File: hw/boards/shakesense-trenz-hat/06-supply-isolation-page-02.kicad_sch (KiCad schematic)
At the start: 9 parts, among them U43 ISO1640BDR

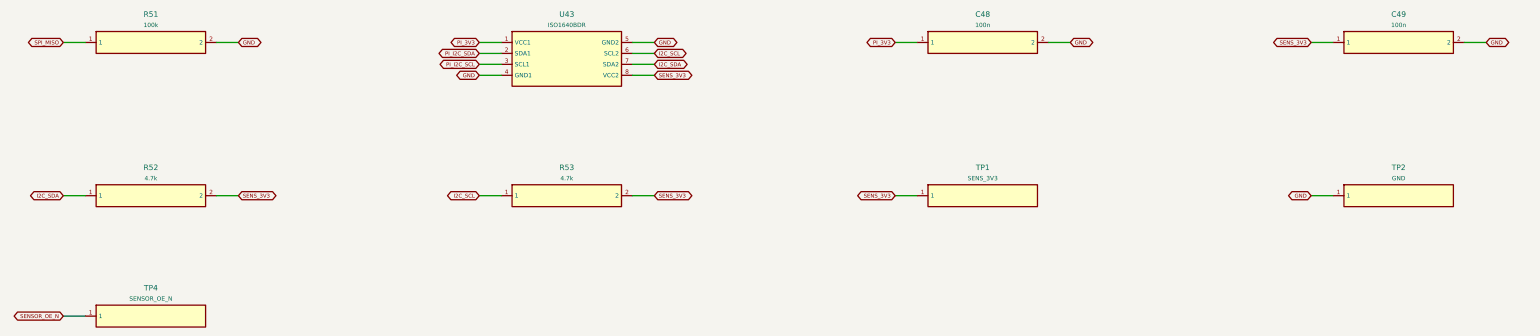
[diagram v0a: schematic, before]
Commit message: Expose Trenz GPIOs on the Pi-outline HDI sensor HAT
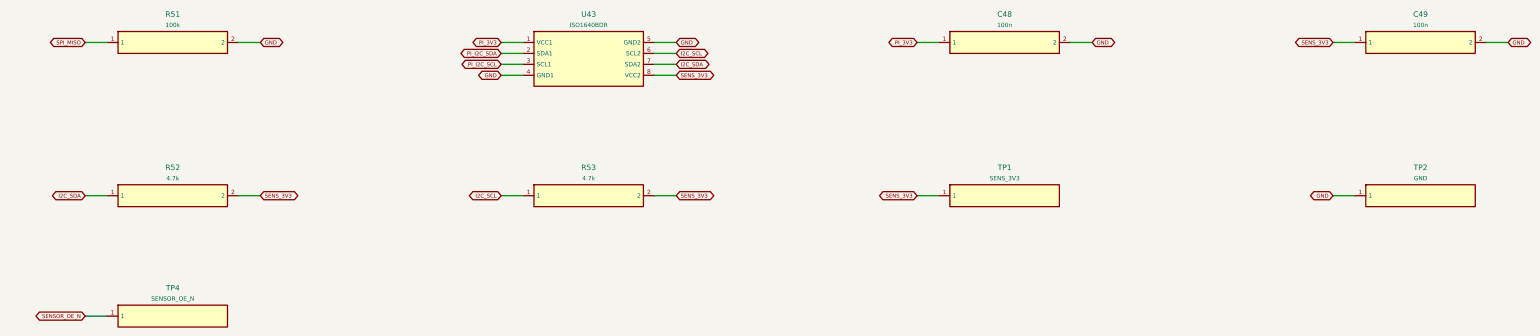
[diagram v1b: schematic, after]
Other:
- title: shakesense-trenz-hat / 06-supply-isolation-page-02 -> ShakeSense T1 / 06-supply-isolation-page-02
- moved on the sheet: C48, C49, R51, R52, R53, TP1, TP2, TP4, U43
